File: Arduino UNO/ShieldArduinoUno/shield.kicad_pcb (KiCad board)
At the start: 4 copper layers, 68.6 x 53.3 mm, 10 parts

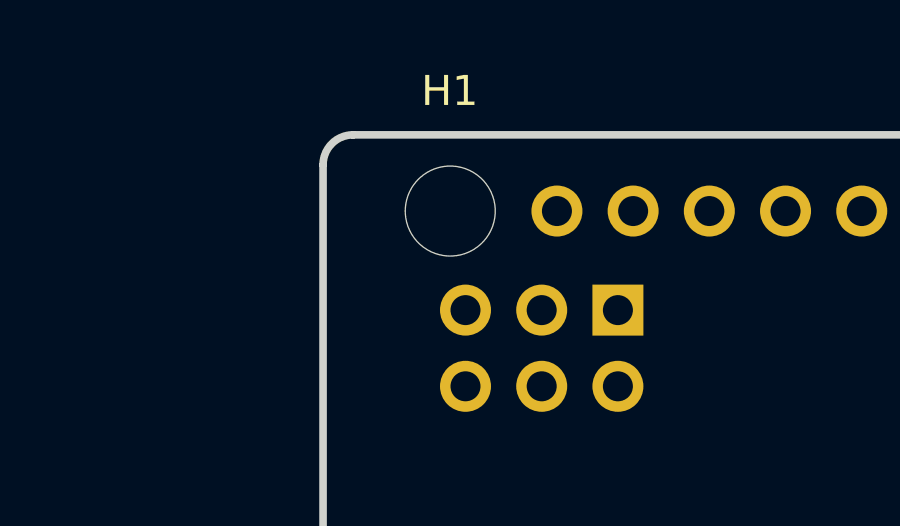
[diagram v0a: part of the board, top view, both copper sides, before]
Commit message: Update shield.kicad_pcb, shield.kicad_pro, and shield.kicad_sch to KiCad 7
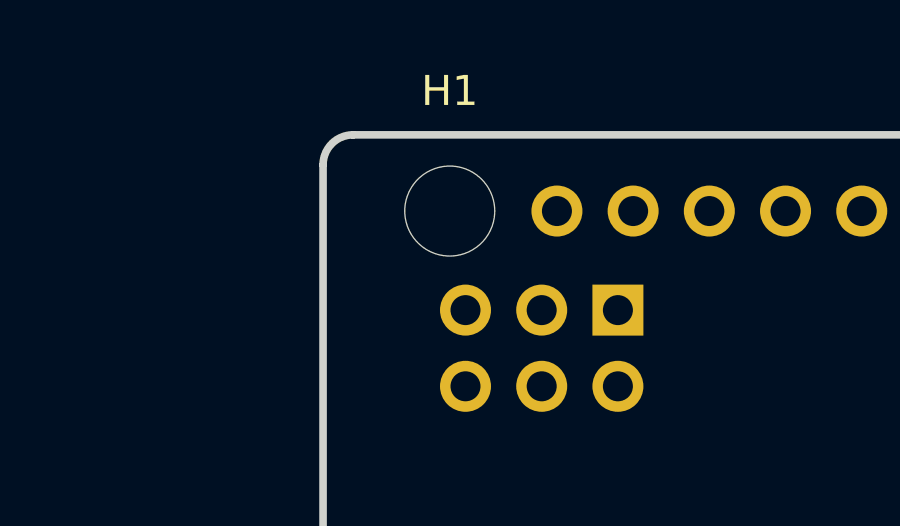
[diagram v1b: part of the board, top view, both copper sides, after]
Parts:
- AD1: value Conn_01x06_Female -> Conn_01x06_Socket
- IOH1: value Conn_01x10_Female -> Conn_01x10_Socket
- IOL1, POWER1: value Conn_01x08_Female -> Conn_01x08_Socket
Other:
- board text removed: "IOL1"

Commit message: REinstated IOREF
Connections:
- net /+5V_Ard_2 renamed /IOREF
